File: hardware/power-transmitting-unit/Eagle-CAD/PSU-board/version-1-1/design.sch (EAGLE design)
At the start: 65 parts, among them IC1 TPL0401A-10DCKR, IC10 TSC1031, IC2 AP7381-50Y-13, IC3 LT8330, IC4 AP7381-33Y-13, IC5 ADS1115IDGST, IC7 TSC1031, IC8 TSC1031, J2 62201021121

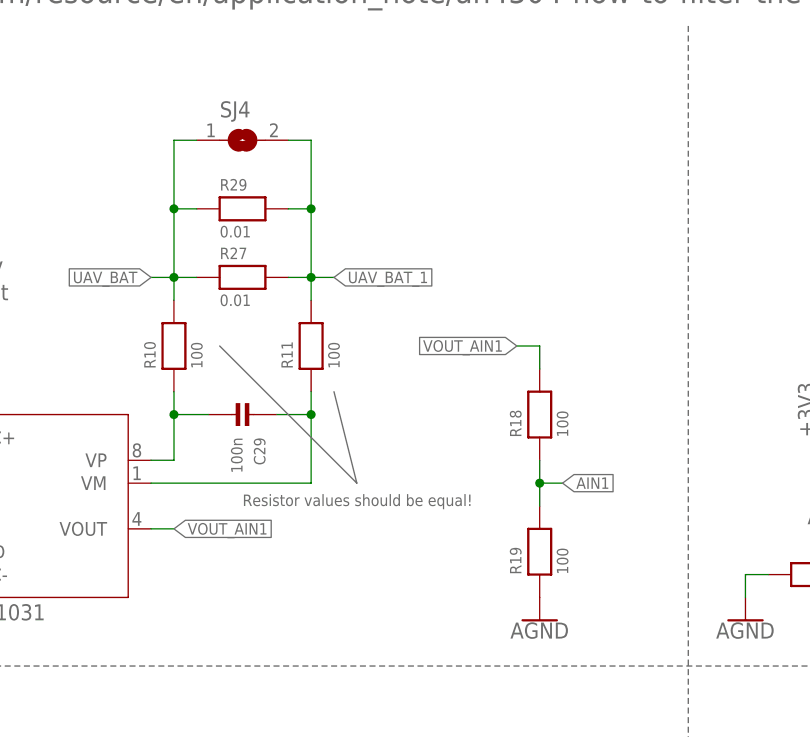
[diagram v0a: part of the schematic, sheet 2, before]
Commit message: Update firmware and reorganization folders
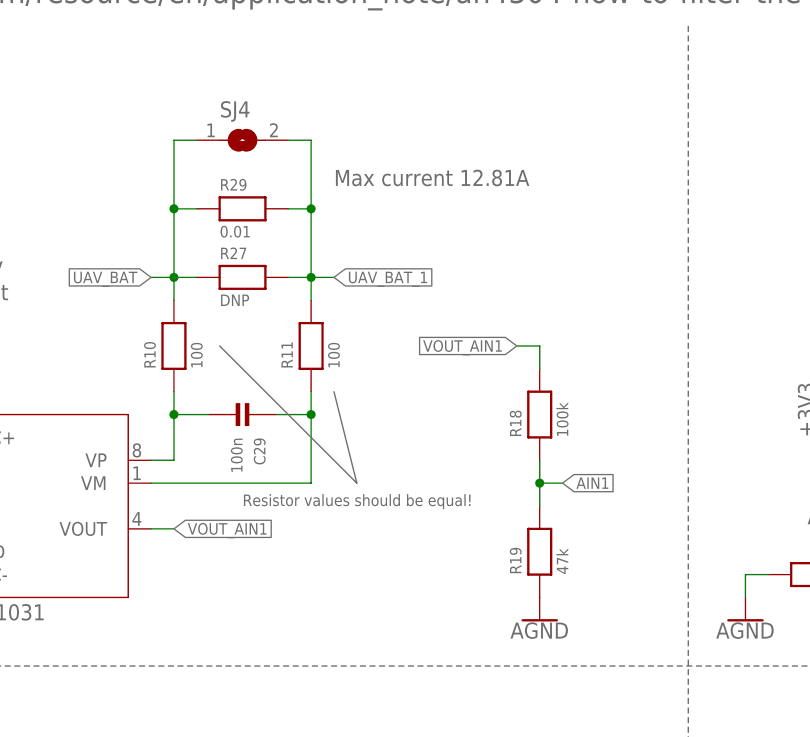
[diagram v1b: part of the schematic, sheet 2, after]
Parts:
- R18: value 100 -> 100k
- R19: value 100 -> 47k
- R27: value 0.01 -> DNP
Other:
- note added: "Max current 12.81A"
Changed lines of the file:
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@@
 <part name="C55" library="microbuilder" deviceset="CAP_CERAMIC" device="0402" value="100n"/>
 <part name="U$47" library="SparkFun-PowerSymbols" deviceset="AGND" device=""/>
-<part name="R27" library="microbuilder" deviceset="RESISTOR" device="0805" value="0.01"/>
+<part name="R27" library="microbuilder" deviceset="RESISTOR" device="0805" value="DNP"/>
 <part name="SJ1" library="SparkFun-Retired" deviceset="SOLDERJUMPER" device="TRACE"/>
 <part name="R28" library="microbuilder" deviceset="RESISTOR" device="0402" value="1k"/>
@@
 <part name="R17" library="microbuilder" deviceset="RESISTOR" device="0402" value="1k"/>
 <part name="U$55" library="SparkFun-PowerSymbols" deviceset="AGND" device=""/>
-<part name="R18" library="microbuilder" deviceset="RESISTOR" device="0603" value="100"/>
-<part name="R19" library="microbuilder" deviceset="RESISTOR" device="0603" value="100"/>
+<part name="R18" library="microbuilder" deviceset="RESISTOR" device="0603" value="100k"/>
+<part name="R19" library="microbuilder" deviceset="RESISTOR" device="0603" value="47k"/>
 <part name="U$56" library="SparkFun-PowerSymbols" deviceset="AGND" device=""/>
 <part name="P+11" library="supply1" library_urn="urn:adsk.eagle:library:371" deviceset="+5V" device=""/>
@@
 <text x="203.2" y="71.12" size="1.778" layer="95">I2C ADDR 0x48</text>
 <text x="203.2" y="71.12" size="1.778" layer="95">I2C ADDR 0x48</text>
+<text x="106.68" y="144.78" size="1.778" layer="95">Max current 12.81A</text>
 </plain>
 <instances>
